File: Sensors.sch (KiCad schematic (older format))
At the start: 11 parts

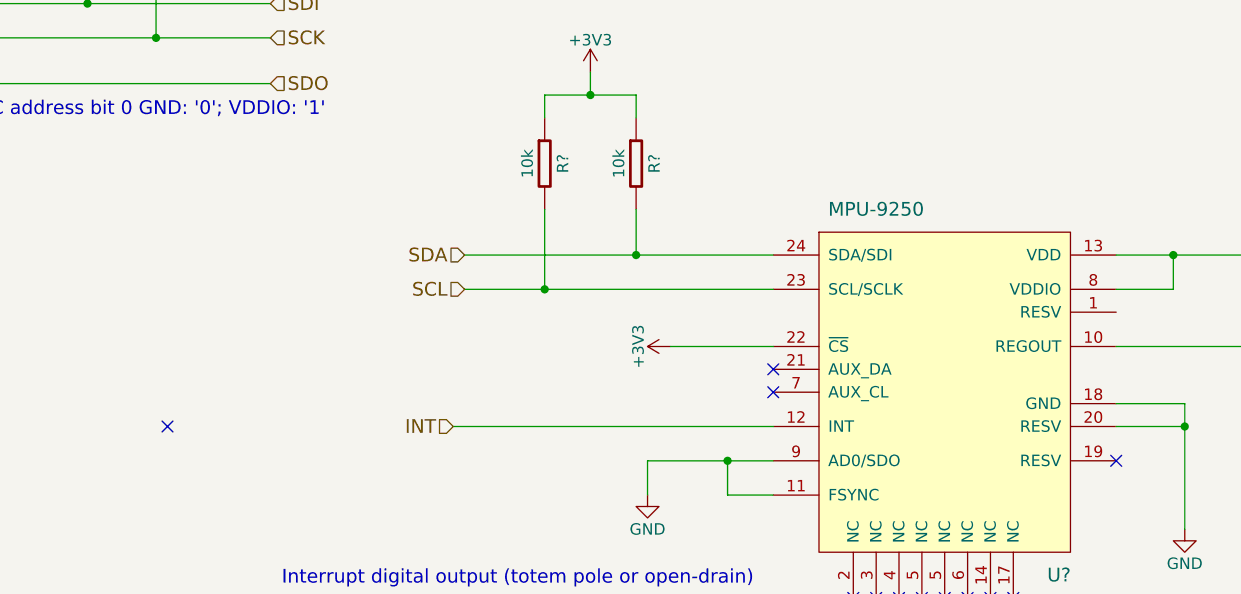
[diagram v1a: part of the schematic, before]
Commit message: 3V8 footprints ergänzt
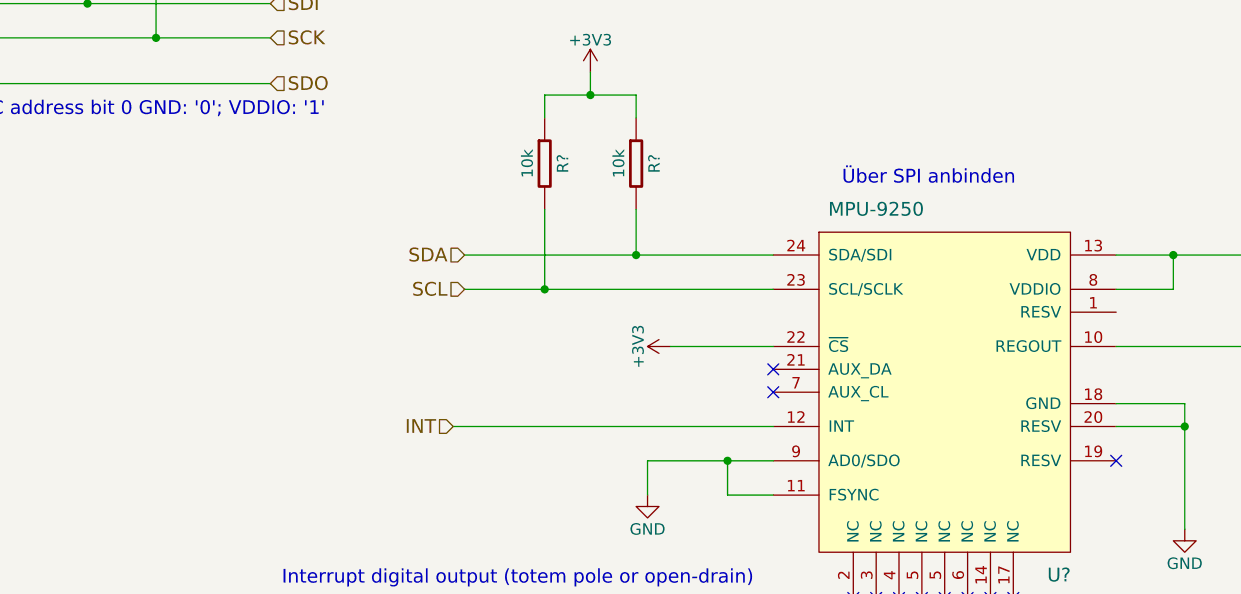
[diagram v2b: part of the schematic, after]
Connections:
- no-connect marks 12 -> 11
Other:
- note added: "Über SPI anbinden\n"
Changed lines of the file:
@@
 $Descr A4 11693 8268
 encoding utf-8
-Sheet 6 8
+Sheet 8 8
 Title ""
 Date ""
@@
 $EndComp
 NoConn ~ 8400 3700
-NoConn ~ 4250 3550
 Wire Wire Line
 	1450 1950 2150 1950
@@
 	1    0    0    -1
 $EndComp
+Text Notes 7200 2500 0    60   ~ 0
+Über SPI anbinden\n
 $EndSCHEMATC

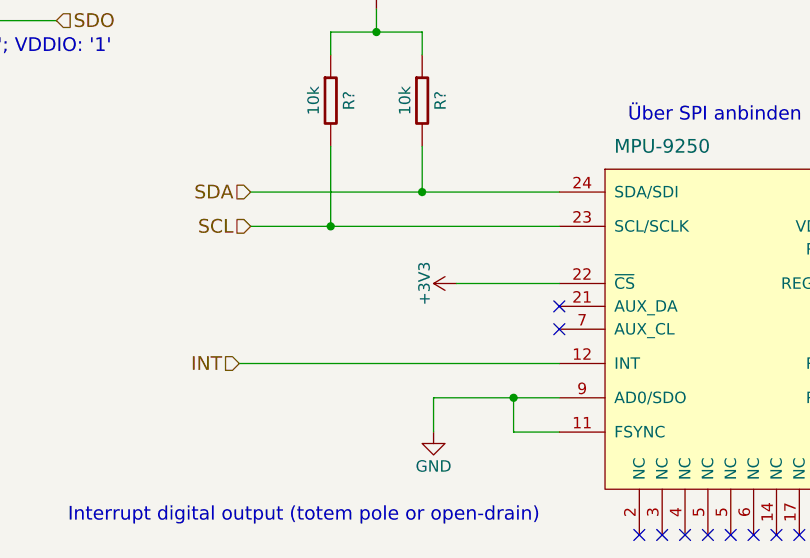
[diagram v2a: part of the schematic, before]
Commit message: NEO N8P durch M8N ersätzt
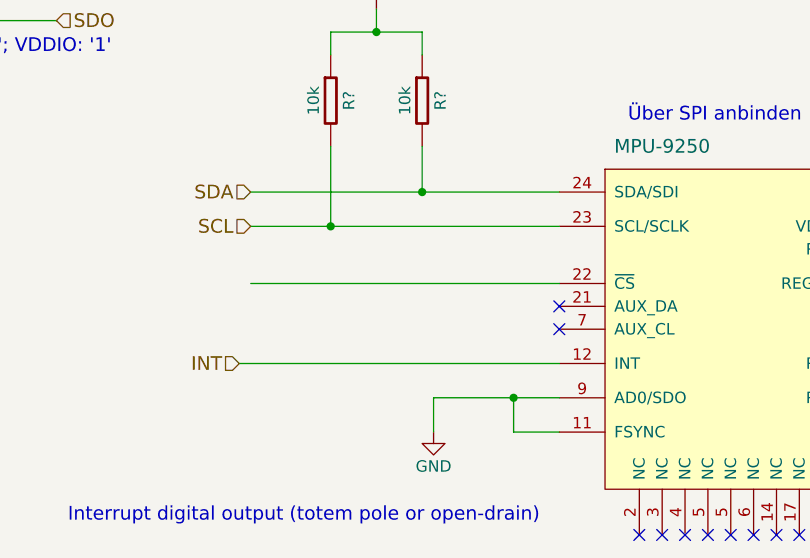
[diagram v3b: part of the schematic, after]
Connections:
- net +3V3: no longer U?.22 (~CS)
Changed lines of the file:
@@
 Text HLabel 5550 2950 0    60   Input ~ 0
 SCL
-$Comp
-L +3V3 #PWR?
-U 1 1 571281D0
-P 6450 3200
-F 0 "#PWR?" H 6450 3050 50  0001 C CNN
-F 1 "+3V3" H 6450 3340 50  0000 C CNN
-F 2 "" H 6450 3200 50  0000 C CNN
-F 3 "" H 6450 3200 50  0000 C CNN
-	1    6450 3200
-	0    -1   -1   0
-$EndComp
-Wire Wire Line
-	6450 3200 6900 3200
 NoConn ~ 6900 3300
 NoConn ~ 6900 3400
@@
 Text Notes 7200 2500 0    60   ~ 0
 Über SPI anbinden\n
+Wire Wire Line
+	6900 3200 5550 3200
 $EndSCHEMATC

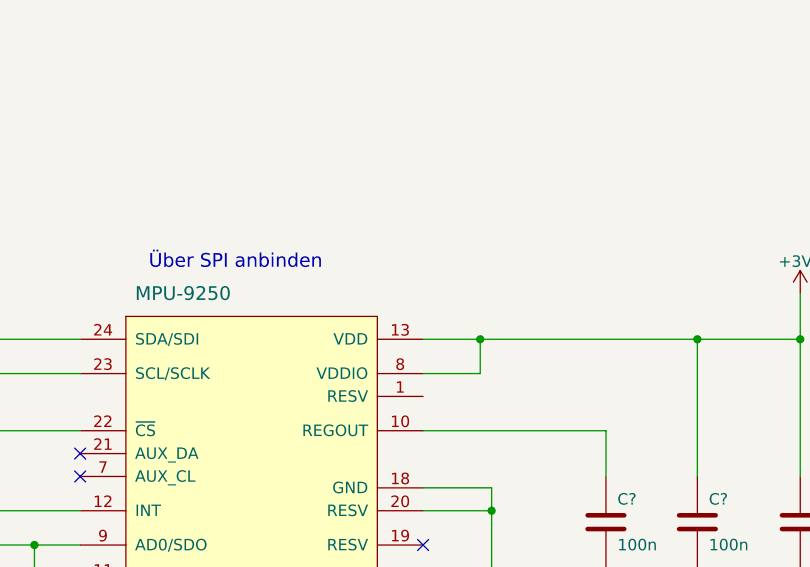
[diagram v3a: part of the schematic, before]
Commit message: footprints ergänzt
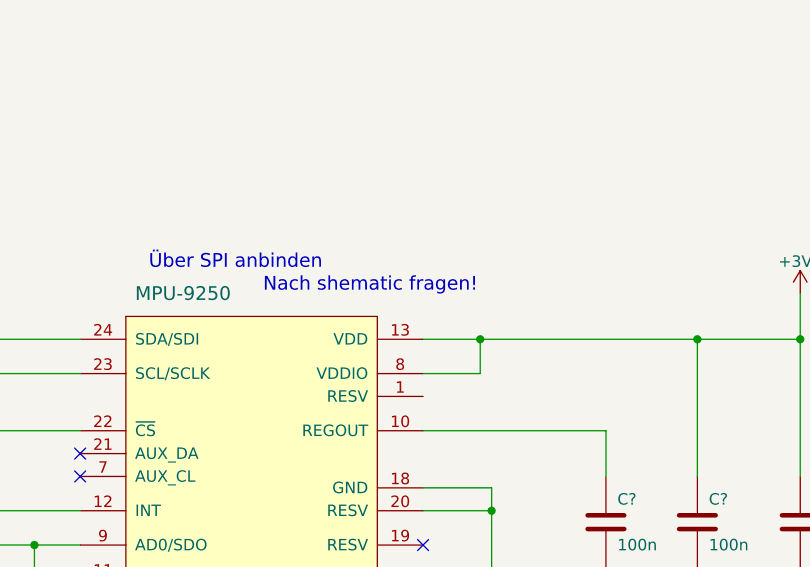
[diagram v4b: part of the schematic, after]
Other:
- note added: "Nach shematic fragen!\n"
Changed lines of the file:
@@
 Wire Wire Line
 	6900 3200 5550 3200
+Text Notes 7700 2600 0    60   ~ 0
+Nach shematic fragen!\n
 $EndSCHEMATC

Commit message: added some footprints
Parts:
- gave numbers to parts that had none: 11
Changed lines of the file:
@@
 $EndDescr
 $Comp
-L BME680 IC?
+L BME680 IC801
 U 1 1 57120309
 P 2700 1500
-F 0 "IC?" H 2400 2050 60  0000 L CNN
+F 0 "IC801" H 2400 2050 60  0000 L CNN
 F 1 "BME680" H 2750 850 60  0000 L CNN
 F 2 "Sensors:BME680" H 1800 -6775 60  0001 C CNN
@@
 $EndComp
 $Comp
-L MPU-9250 U?
+L MPU-9250 U801
 U 1 1 571208B7
 P 7650 3550
-F 0 "U?" H 8150 2900 60  0000 C CNN
+F 0 "U801" H 8150 2900 60  0000 C CNN
 F 1 "MPU-9250" H 7350 4500 60  0000 C CNN
 F 2 "Sensors:MPU-9250" H 7600 3800 60  0001 C CNN
@@
 $EndComp
 $Comp
-L C C?
+L C C801
 U 1 1 571208F8
 P 1450 1400
-F 0 "C?" H 1500 1500 50  0000 L CNN
+F 0 "C801" H 1500 1500 50  0000 L CNN
 F 1 "100n" H 1500 1300 50  0000 L CNN
 F 2 "Passives:C0402N" H 1488 1250 30  0001 C CNN
@@
 $EndComp
 $Comp
-L C C?
+L C C802
 U 1 1 5712093B
 P 1750 1400
-F 0 "C?" H 1800 1500 50  0000 L CNN
+F 0 "C802" H 1800 1500 50  0000 L CNN
 F 1 "100n" H 1800 1300 50  0000 L CNN
 F 2 "Passives:C0402N" H 1788 1250 30  0001 C CNN
@@
 $EndComp
 $Comp
-L +3V3 #PWR?
+L +3V3 #PWR0171
 U 1 1 5712095D
 P 1450 1000
-F 0 "#PWR?" H 1450 850 50  0001 C CNN
+F 0 "#PWR0171" H 1450 850 50  0001 C CNN
 F 1 "+3V3" H 1450 1140 50  0000 C CNN
 F 2 "" H 1450 1000 50  0000 C CNN
@@
 $EndComp
 $Comp
-L GND #PWR?
+L GND #PWR0172
 U 1 1 5712097D
 P 1450 2000
-F 0 "#PWR?" H 1450 1750 50  0001 C CNN
+F 0 "#PWR0172" H 1450 1750 50  0001 C CNN
 F 1 "GND" H 1450 1850 50  0000 C CNN
 F 2 "" H 1450 2000 50  0000 C CNN
@@
 	1750 1200 1750 1100
 $Comp
-L R R?
+L R R801
 U 1 1 57120A95
 P 3900 1400
-F 0 "R?" V 3980 1400 50  0000 C CNN
+F 0 "R801" V 3980 1400 50  0000 C CNN
 F 1 "4,7k" V 3825 1400 50  0000 C CNN
 F 2 "Passives:R0402N" V 3830 1400 30  0001 C CNN
@@
 $EndComp
 $Comp
-L R R?
+L R R802
 U 1 1 57120AC6
 P 4200 1400
-F 0 "R?" V 4280 1400 50  0000 C CNN
+F 0 "R802" V 4280 1400 50  0000 C CNN
 F 1 "4,7k" V 4125 1400 50  0000 C CNN
 F 2 "Passives:R0402N" V 4130 1400 30  0001 C CNN
@@
 	4200 1600 4200 1850
 $Comp
-L R R?
+L R R804
 U 1 1 571216FF
 P 6300 2400
-F 0 "R?" V 6380 2400 50  0000 C CNN
+F 0 "R804" V 6380 2400 50  0000 C CNN
 F 1 "10k" V 6225 2400 50  0000 C CNN
 F 2 "Passives:R0402N" V 6230 2400 30  0001 C CNN
@@
 	9200 3200 9200 3400
 $Comp
-L GND #PWR?
+L GND #PWR0173
 U 1 1 57122FCF
 P 8700 4000
-F 0 "#PWR?" H 8700 3750 50  0001 C CNN
+F 0 "#PWR0173" H 8700 3750 50  0001 C CNN
 F 1 "GND" H 8700 3850 50  0000 C CNN
 F 2 "" H 8700 4000 50  0000 C CNN
@@
 $EndComp
 $Comp
-L GND #PWR?
+L GND #PWR0174
 U 1 1 57123008
 P 9200 4000
-F 0 "#PWR?" H 9200 3750 50  0001 C CNN
+F 0 "#PWR0174" H 9200 3750 50  0001 C CNN
 F 1 "GND" H 9200 3850 50  0000 C CNN
 F 2 "" H 9200 4000 50  0000 C CNN
@@
 	9200 3800 9200 4000
 $Comp
-L +3V3 #PWR?
+L +3V3 #PWR0175
 U 1 1 57123302
 P 10050 2600
-F 0 "#PWR?" H 10050 2450 50  0001 C CNN
+F 0 "#PWR0175" H 10050 2450 50  0001 C CNN
 F 1 "+3V3" H 10050 2740 50  0000 C CNN
 F 2 "" H 10050 2600 50  0000 C CNN
@@
 Connection ~ 8650 2800
 $Comp
-L GND #PWR?
+L GND #PWR0176
 U 1 1 571235AC
 P 9600 4000
-F 0 "#PWR?" H 9600 3750 50  0001 C CNN
+F 0 "#PWR0176" H 9600 3750 50  0001 C CNN
 F 1 "GND" H 9600 3850 50  0000 C CNN
 F 2 "" H 9600 4000 50  0000 C CNN
@@
 $EndComp
 $Comp
-L GND #PWR?
+L GND #PWR0177
 U 1 1 571235FC
 P 10050 4000
-F 0 "#PWR?" H 10050 3750 50  0001 C CNN
+F 0 "#PWR0177" H 10050 3750 50  0001 C CNN
 F 1 "GND" H 10050 3850 50  0000 C CNN
 F 2 "" H 10050 4000 50  0000 C CNN
@@
 	9600 3800 9600 4000
 $Comp
-L +3V3 #PWR?
+L +3V3 #PWR0178
 U 1 1 57127673
 P 6100 2000
-F 0 "#PWR?" H 6100 1850 50  0001 C CNN
+F 0 "#PWR0178" H 6100 1850 50  0001 C CNN
 F 1 "+3V3" H 6100 2140 50  0000 C CNN
 F 2 "" H 6100 2000 50  0000 C CNN
@@
 NoConn ~ 6900 3400
 $Comp
-L GND #PWR?
+L GND #PWR0179
 U 1 1 5712831A
 P 6350 3850
-F 0 "#PWR?" H 6350 3600 50  0001 C CNN
+F 0 "#PWR0179" H 6350 3600 50  0001 C CNN
 F 1 "GND" H 6350 3700 50  0000 C CNN
 F 2 "" H 6350 3850 50  0000 C CNN
@@
 Interrupt digital output (totem pole or open-drain) \n
 $Comp
-L C C?
+L C C803
 U 1 1 57129277
 P 9200 3600
-F 0 "C?" H 9250 3700 50  0000 L CNN
+F 0 "C803" H 9250 3700 50  0000 L CNN
 F 1 "100n" H 9250 3500 50  0000 L CNN
 F 2 "Passives:C0402N" H 9238 3450 30  0001 C CNN
@@
 Connection ~ 3900 1100
 $Comp
-L +3V3 #PWR?
+L +3V3 #PWR0180
 U 1 1 57110B2A
 P 4200 900
-F 0 "#PWR?" H 4200 750 50  0001 C CNN
+F 0 "#PWR0180" H 4200 750 50  0001 C CNN
 F 1 "+3V3" H 4200 1040 50  0000 C CNN
 F 2 "" H 4200 900 50  0000 C CNN
@@
 SDO
 $Comp
-L R R?
+L R R803
 U 1 1 57116F68
 P 5900 2400
-F 0 "R?" V 5980 2400 50  0000 C CNN
+F 0 "R803" V 5980 2400 50  0000 C CNN
 F 1 "10k" V 5825 2400 50  0000 C CNN
 F 2 "Passives:R0402N" V 5830 2400 30  0001 C CNN
@@
 $EndComp
 $Comp
-L C C?
+L C C804
 U 1 1 57117060
 P 9600 3600
-F 0 "C?" H 9650 3700 50  0000 L CNN
+F 0 "C804" H 9650 3700 50  0000 L CNN
 F 1 "100n" H 9650 3500 50  0000 L CNN
 F 2 "Passives:C0402N" H 9638 3450 30  0001 C CNN
@@
 $EndComp
 $Comp
-L C C?
+L C C805
 U 1 1 57117099
 P 10050 3600
-F 0 "C?" H 10100 3700 50  0000 L CNN
+F 0 "C805" H 10100 3700 50  0000 L CNN
 F 1 "100n" H 10100 3500 50  0000 L CNN
 F 2 "Passives:C0402N" H 10088 3450 30  0001 C CNN
